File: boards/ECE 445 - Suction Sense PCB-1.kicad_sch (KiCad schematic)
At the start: 44 parts, among them J1 Paddle Sensor, J2 Motion Sensor, J3 Battery Connector, J4 Barrel_Jack, U1 ESP32-WROOM-32E, U2 TPS2121RUXR, U3 AP62150Z6, U4 MCP73831-2-OT, U5 TPS61222DCKR

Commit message: changed schematic and baord
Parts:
- added C11: 22uf, Capacitor_SMD:C_0805_2012Metric_Pad1.18x1.45mm_HandSolder, symbol Device:C
- added C12: 0.1uf, Capacitor_SMD:C_0805_2012Metric_Pad1.18x1.45mm_HandSolder, symbol Device:C
- added C13: 1uf, Capacitor_SMD:C_0805_2012Metric_Pad1.18x1.45mm_HandSolder, symbol Device:C
- added J5: Conn_01x06_Pin, Connector_Molex:Molex_KK-396_A-41791-0006_1x06_P3.96mm_Vertical, symbol Connector:Conn_01x06_Pin
- added R14: R, Resistor_SMD:R_0805_2012Metric_Pad1.20x1.40mm_HandSolder, symbol Device:R
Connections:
- net 3v3: now also C11.1, C12.1, R14.2
- net BUCK_IN: now also U3.5 (EN)
- net GND: now also C11.2, C12.2, C13.1, J5.1 (Pin_1)
- net at U1.25 (IO0): now also J5.4 (Pin_4)
- net at U1.3 (EN): now also C13.2, J5.5 (Pin_5), R14.1
- net at U1.34 (RXD0/IO3): now also J5.2 (Pin_2)
- net at U1.35 (TXD0/IO1): now also J5.3 (Pin_3)
- net EN renamed IO34
- net IO34: no longer U3.5 (EN)

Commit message: new baord
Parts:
- removed R11: 100K, Resistor_SMD:R_0805_2012Metric_Pad1.20x1.40mm_HandSolder, symbol Device:R
- U3: footprint Package_TO_SOT_SMD:SOT-563 -> Package_TO_SOT_SMD:TSOT-23-6_HandSoldering
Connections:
- net +3.7VA: now also U5.6 (EN)
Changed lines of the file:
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@@
 	(wire
 		(pts
+			(xy 95.25 119.38) (xy 95.25 129.54)
+		)
+		(stroke
+			(width 0)
+			(type default)
+		)
+	)
+	(wire
+		(pts
 			(xy 214.63 129.54) (xy 214.63 130.81)
 		)
@@
 	(wire
 		(pts
-			(xy 95.25 119.38) (xy 95.25 121.92)
-		)
-		(stroke
-			(width 0)
-			(type default)
-		)
-	)
-	(wire
-		(pts
 			(xy 102.87 41.91) (xy 102.87 43.18)
 		)
@@
 			)
 		)
-		(property "Footprint" "Package_TO_SOT_SMD:SOT-563"
+		(property "Footprint" "Package_TO_SOT_SMD:TSOT-23-6_HandSoldering"
 			(at 195.58 142.24 0)
 			(effects
@@
 					(unit 1)
 				)
-			)
-		)
-	)
-	(symbol
-		(lib_id "Device:R")
-		(at 95.25 125.73 0)
-		(unit 1)
-		(exclude_from_sim no)
-		(in_bom yes)
-		(on_board yes)
-		(dnp no)
-		(fields_autoplaced yes)
-		(property "Reference" "R11"
-			(at 97.79 124.4599 0)
-			(effects
-				(font
-					(size 1.27 1.27)
-				)
-				(justify left)
-			)
-		)
-		(property "Value" "100K"
-			(at 97.79 126.9999 0)
-			(effects
-				(font
-					(size 1.27 1.27)
-				)
-				(justify left)
-			)
-		)
-		(property "Footprint" "Resistor_SMD:R_0805_2012Metric_Pad1.20x1.40mm_HandSolder"
-			(at 93.472 125.73 90)
-			(effects
-				(font
-					(size 1.27 1.27)
-				)
-				(hide yes)
-			)
-		)
-		(property "Datasheet" "~"
-			(at 95.25 125.73 0)
-			(effects
-				(font
-					(size 1.27 1.27)
-				)
-				(hide yes)
-			)
-		)
-		(property "Description" "Resistor"
-			(at 95.25 125.73 0)
-			(effects
-				(font
-					(size 1.27 1.27)
-				)
-				(hide yes)
-			)
-		)
-		(pin "2"
-		)
-		(pin "1"
-		)
-		(instances
-			(project ""
-				(path "/561ea10a-797a-46d1-9f30-325f0302a4a7"
-					(reference "R11")
-					(unit 1)
-				)

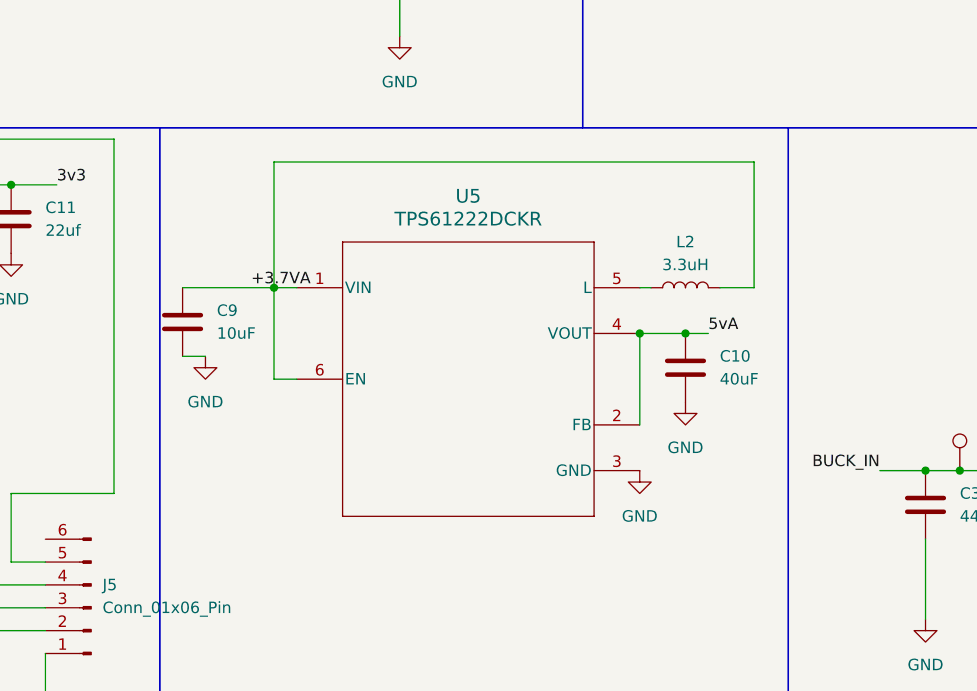
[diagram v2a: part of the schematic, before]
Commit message: better footprint for boost
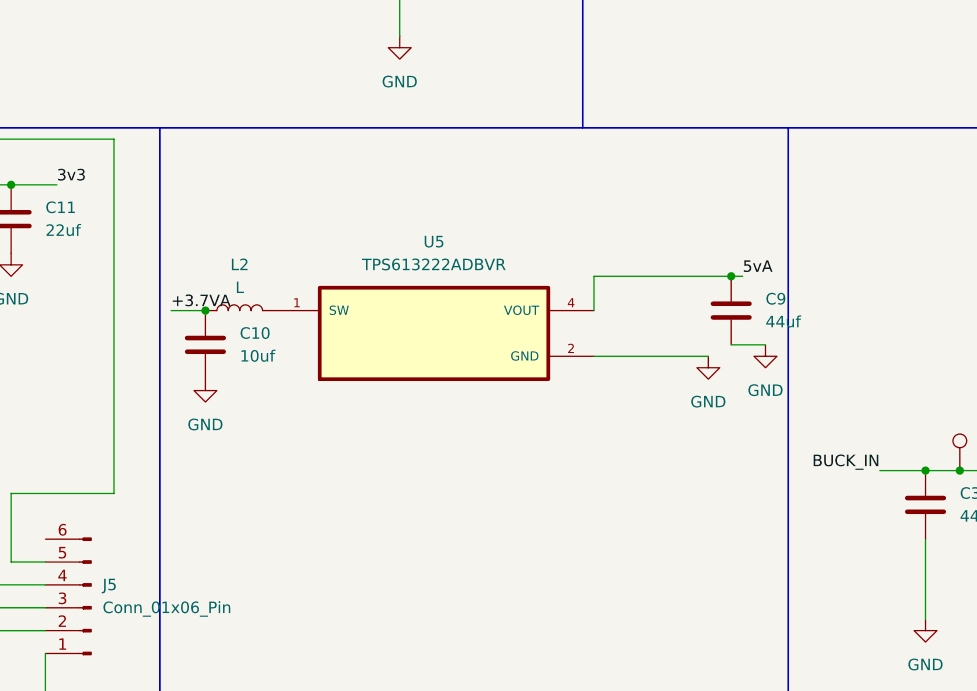
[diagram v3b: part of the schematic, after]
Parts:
- removed U5: TPS61222DCKR, KiCadExtras:DCK0006A, symbol 2025-10-12_01-10-01:TPS61222DCKR
- added U5: TPS613222ADBVR, KiCadExtras:SOT95P280X145-5N, symbol TPS613:TPS613222ADBVR
- C10: value 40uF -> 10uf
- C9: value 10uF -> 44uf
- L1: footprint Inductor_SMD:L_0805_2012Metric_Pad1.15x1.40mm_HandSolder -> Inductor_SMD:L_Changjiang_FTC201655S
- L2: value 3.3uH -> L; footprint Inductor_SMD:L_0805_2012Metric_Pad1.15x1.40mm_HandSolder -> Inductor_SMD:L_Changjiang_FTC201655S
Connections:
- net +3.7VA: now also C10.1, L2.1; no longer C9.1, L2.2
- net 5vA: now also C9.1, U5.4 (VOUT); no longer C10.1
- net GND: now also U5.2 (GND)
- new net: L2.2, U5.1 (SW)

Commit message: new upadtes to board
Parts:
- L2: value L -> 2.2uH
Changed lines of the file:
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@@
+	)
+	(junction
+		(at 102.87 48.26)
+		(diameter 0)
+		(color 0 0 0 0)
+	)
+	(junction
+		(at 54.61 107.95)
+		(diameter 0)
+		(color 0 0 0 0)
+	)
+	(junction
+		(at 223.52 138.43)
+		(diameter 0)
+		(color 0 0 0 0)
+	)
+	(junction
+		(at 58.42 41.91)
+		(diameter 0)
+		(color 0 0 0 0)
+	)
+	(junction
+		(at 214.63 138.43)
+		(diameter 0)
+		(color 0 0 0 0)
+	)
+	(junction
+		(at 247.65 125.73)
+		(diameter 0)
+		(color 0 0 0 0)
+	)
+	(junction
+		(at 40.64 110.49)
+		(diameter 0)
+		(color 0 0 0 0)
 	)
 	(junction
@@
 	)
 	(junction
-		(at 102.87 48.26)
-		(diameter 0)
-		(color 0 0 0 0)
-	)
-	(junction
-		(at 54.61 107.95)
-		(diameter 0)
-		(color 0 0 0 0)
-	)
-	(junction
-		(at 223.52 138.43)
-		(diameter 0)
-		(color 0 0 0 0)
-	)
-	(junction
-		(at 58.42 41.91)
-		(diameter 0)
-		(color 0 0 0 0)
-	)
-	(junction
-		(at 214.63 138.43)
-		(diameter 0)
-		(color 0 0 0 0)
-	)
-	(junction
-		(at 247.65 125.73)
-		(diameter 0)
-		(color 0 0 0 0)
-	)
-	(junction
-		(at 40.64 110.49)
-		(diameter 0)
-		(color 0 0 0 0)
-	)
-	(junction
 		(at 167.64 139.7)
 		(diameter 0)
@@
 	(wire
 		(pts
+			(xy 27.94 33.02) (xy 35.56 33.02)
+		)
+		(stroke
+			(width 0)
+			(type default)
+		)
+	)
+	(wire
+		(pts
 			(xy 130.81 121.92) (xy 130.81 118.11)
-		)
-		(stroke
-			(width 0)
-			(type default)
-		)
-	)
-	(wire
-		(pts
-			(xy 27.94 33.02) (xy 35.56 33.02)
 		)
 		(stroke
@@
 			)
 		)
-		(property "Value" "L"
+		(property "Value" "2.2uH"
 			(at 91.44 119.38 90)
 			(effects
@@
 		(on_board yes)
 		(dnp no)
-		(fields_autoplaced yes)
 		(property "Reference" "#PWR015"
 			(at 24.13 34.29 0)
@@
 		)
 		(property "Value" "GND"
-			(at 24.13 33.02 0)
-			(effects
-				(font
+			(at 21.59 30.48 0)
+			(effects
+				(font
